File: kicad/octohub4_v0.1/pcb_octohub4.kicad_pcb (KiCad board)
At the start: 2 copper layers, 100 x 80 mm, 83 parts, among them J101 USB231ARY, J102 USB231ARY, J103 USB231ARY, J104 USB231ARY, J201 Screw_Terminal_01x02, J203 Barrel_Jack_Switch, J301 USB_C_Receptacle_USB2.0, U201 TPS259474LRPWR, U301 AMS1117-3.3, U302 USB2514B_Bi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

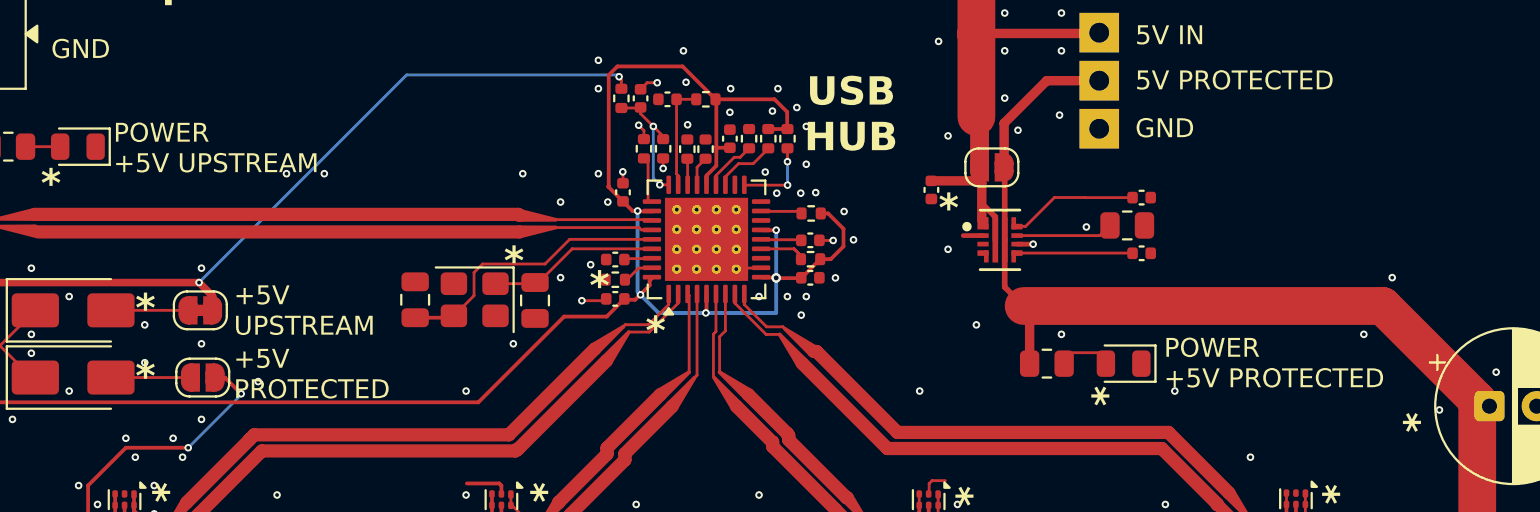
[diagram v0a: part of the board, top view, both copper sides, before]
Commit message: Add run_kicad_purge 8
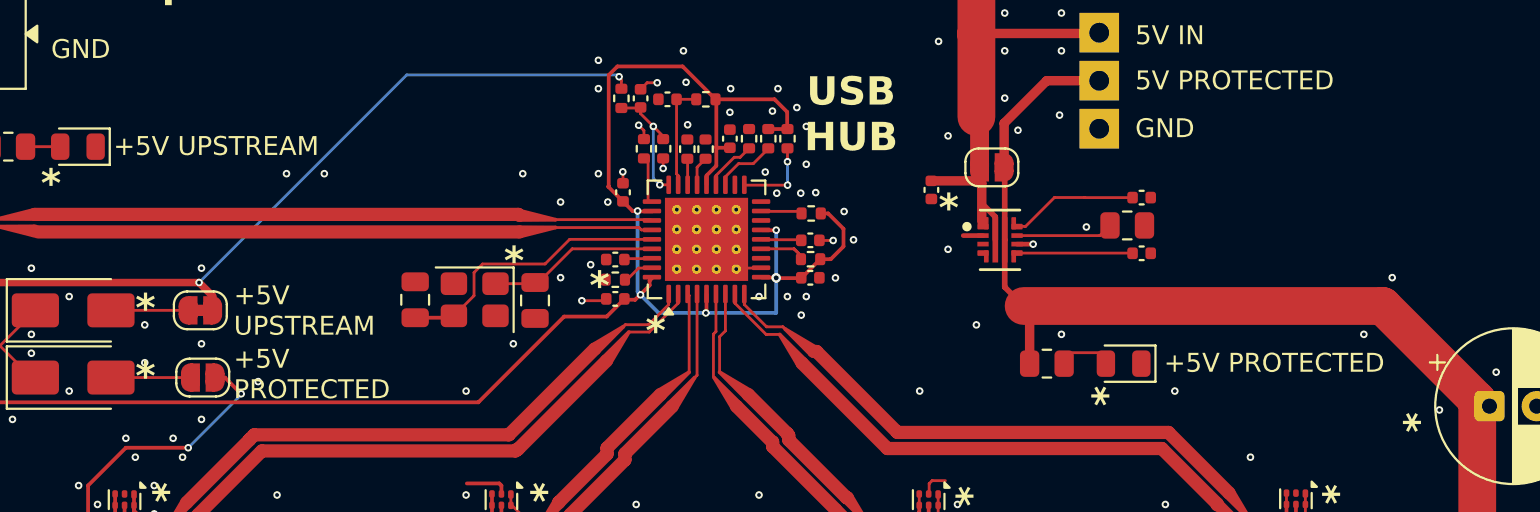
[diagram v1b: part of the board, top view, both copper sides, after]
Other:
- board text removed: "POWER +5V PROTECTED"
- board text removed: "POWER +5V UPSTREAM"
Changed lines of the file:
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@@
 			)
 		)
-		(property "Description" "19.414.67.1mm USB Connectors ROHS 4 pin USB 2.0 DC 30V 1.5 A"
+		(property "Description" "USB Connectors ROHS 4 pin USB 2.0 DC 30V 1.5 A"
 			(at 0 0 0)
 			(unlocked yes)
@@
 			)
 		)
-		(property "Datasheet_alt" "https://datasheet.lcsc.com/lcsc/2008111235_XUNPU-USB-226-BRW_C720524.pdf"
+		(property "Datasheet_alt" "https://jlcpcb.com/api/file/downloadByFileSystemAccessId/8608741080523153408"
 			(at 0 0 0)
 			(unlocked yes)
@@
 			)
 		)
-		(property "Description" "19.414.67.1mm USB Connectors ROHS 4 pin USB 2.0 DC 30V 1.5 A"
+		(property "Description" "USB Connectors ROHS 4 pin USB 2.0 DC 30V 1.5 A"
 			(at 0 0 0)
 			(unlocked yes)
@@
 			)
 		)
-		(property "Datasheet_alt" "https://datasheet.lcsc.com/lcsc/2008111235_XUNPU-USB-226-BRW_C720524.pdf"
+		(property "Datasheet_alt" "https://jlcpcb.com/api/file/downloadByFileSystemAccessId/8608741080523153408"
 			(at 0 0 0)
 			(unlocked yes)
@@
 			)
 		)
-		(property "Description" "19.414.67.1mm USB Connectors ROHS 4 pin USB 2.0 DC 30V 1.5 A"
+		(property "Description" "USB Connectors ROHS 4 pin USB 2.0 DC 30V 1.5 A"
 			(at 0 0 0)
 			(unlocked yes)
@@
 			)
 		)
-		(property "Datasheet_alt" "https://datasheet.lcsc.com/lcsc/2008111235_XUNPU-USB-226-BRW_C720524.pdf"
+		(property "Datasheet_alt" "https://jlcpcb.com/api/file/downloadByFileSystemAccessId/8608741080523153408"
 			(at 0 0 0)
 			(unlocked yes)
@@
 			)
 		)
-		(property "Description" "19.414.67.1mm USB Connectors ROHS 4 pin USB 2.0 DC 30V 1.5 A"
+		(property "Description" "USB Connectors ROHS 4 pin USB 2.0 DC 30V 1.5 A"
 			(at 0 0 0)
 			(unlocked yes)
@@
 			)
 		)
-		(property "Datasheet_alt" "https://datasheet.lcsc.com/lcsc/2008111235_XUNPU-USB-226-BRW_C720524.pdf"
+		(property "Datasheet_alt" "https://jlcpcb.com/api/file/downloadByFileSystemAccessId/8608741080523153408"
 			(at 0 0 0)
 			(unlocked yes)
@@
 		)
 	)
-	(gr_text "POWER\n+5V PROTECTED"
-		(at 133.18 74.68 0)
+	(gr_text "+5V PROTECTED"
+		(at 133.18 73.86 0)
 		(layer "F.SilkS")
 		(effects
@@
 		)
 	)
-	(gr_text "POWER\n+5V UPSTREAM"
-		(at 77.6 63.3 0)
+	(gr_text "+5V UPSTREAM"
+		(at 77.6 62.39 0)
 		(layer "F.SilkS")
 		(effects

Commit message: Add run_kicad_purge 9
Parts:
- added D208: green, LED_SMD:LED_0805_2012Metric, F.Cu at (127.0, 73.8)
- added R203: 4K7, Resistor_SMD:R_0805_2012Metric, F.Cu at (131.1, 73.8)
- moved R202 4.42 mm to (131.1, 71.6), turned to 0 degrees
- moved D207 4.35 mm to (127.0, 71.6), turned to 0 degrees
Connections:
- U201 pad 4: unconnected-(U201-PGTH-Pad4) -> Net-(D208-K)
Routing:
- net Net-(D208-K): track 0.00 -> 8.39 mm
- net Net-(D208-A): track 0.00 -> 2.21 mm
- net +5VPROTECTED: track 203.9 -> 205.3 mm
- net GND: vias 216 -> 226
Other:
- board text added: "FAULT"

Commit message: Version v0.1
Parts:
- R201: value 120 -> 680
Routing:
- net +5VIN: track 256.6 -> 255.9 mm
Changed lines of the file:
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@@
 			)
 		)
-		(property "KiCadOriginal" "MountingHole_3.2mm_M3_DIN965_Pad"
-			(at 0 0 0)
-			(layer "F.SilkS")
-			(hide yes)
-			(effects
-				(font
-					(size 1 1)
-					(thickness 0.1)
-				)
-			)
-		)
 		(property ki_fp_filters "MountingHole*Pad*")
 		(sheetname "/Power Protection/")
@@
 			)
 		)
-		(property "KiCadOriginal" "MountingHole_3.2mm_M3_DIN965_Pad"
-			(at 0 0 0)
-			(layer "F.SilkS")
-			(hide yes)
-			(effects
-				(font
-					(size 1 1)
-					(thickness 0.1)
-				)
-			)
-		)
 		(property ki_fp_filters "MountingHole*Pad*")
 		(sheetname "/Power Protection/")
@@
 			)
 		)
-		(property "KiCadOriginal" "TerminalBlock_WAGO_236-402_1x02_P5.00mm_45Degree"
-			(at 0 0 90)
-			(layer "F.SilkS")
-			(hide yes)
-			(effects
-				(font
-					(size 1 1)
-					(thickness 0.1)
-				)
-			)
-		)
 		(property ki_fp_filters "TerminalBlock*:*")
 		(sheetname "/Power Protection/")
@@
 			)
 		)
-		(property "KiCadOrigin" "BarrelJack_CUI_PJ-079BH_Horizontal"
-			(at 0 0 90)
-			(layer "F.SilkS")
-			(hide yes)
-			(effects
-				(font
-					(size 1 1)
-					(thickness 0.1)
-				)
-			)
-		)
 		(property "JLCPCB" "C319095"
 			(at 0 0 270)
@@
 			)
 		)
-		(property "Value" "120"
+		(property "Value" "680"
 			(at 0 1.65 0)
 			(layer "F.Fab")
@@
 			)
 		)
-		(property "KiCadOriginal" "MountingHole_3.2mm_M3_DIN965_Pad"
-			(at 0 0 0)
-			(layer "F.SilkS")
-			(hide yes)
-			(effects
-				(font
-					(size 1 1)
-					(thickness 0.1)
-				)
-			)
-		)
 		(property ki_fp_filters "MountingHole*Pad*")
 		(sheetname "/Power Protection/")
@@
 			)
 		)
-		(property "KiCadOriginal" "MountingHole_3.2mm_M3_DIN965_Pad"
-			(at 0 0 0)
-			(layer "F.SilkS")
-			(hide yes)
-			(effects
-				(font
-					(size 1 1)
-					(thickness 0.1)
-				)
-			)
-		)
 		(property ki_fp_filters "MountingHole*Pad*")
 		(sheetname "/Power Protection/")
@@
 	)
 	(segment
-		(start 124.26 65.99)
-		(end 124.26 66.4)
-		(width 0.3)
-		(layer "F.Cu")
-		(net 1)
-	)
-	(segment
 		(start 123.4432 63.6612)
 		(end 123.5448 63.7628)
@@
 	)
 	(segment
-		(start 124.26 66.4)
-		(end 124.26 66.76)
-		(width 0.3)
-		(layer "F.Cu")
-		(net 1)
-	)
-	(segment
 		(start 72.41 23.26)
 		(end 73.76 23.26)
@@
 		(layer "F.Cu")
 		(net 2)
-	)
-	(segment
-		(start 131.9825 73.7875)
-		(end 131.9925 73.7775)
-		(width 0.5)
-		(layer "F.Cu")
-		(net 2)

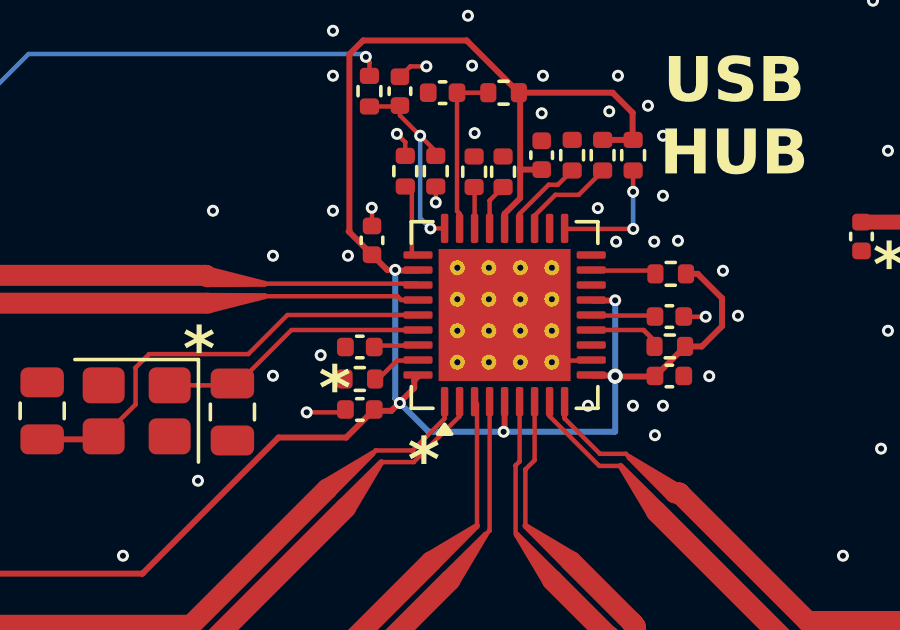
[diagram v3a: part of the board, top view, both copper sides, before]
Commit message: New via constraints: Copy usb hub footprint from tentacle v0.7
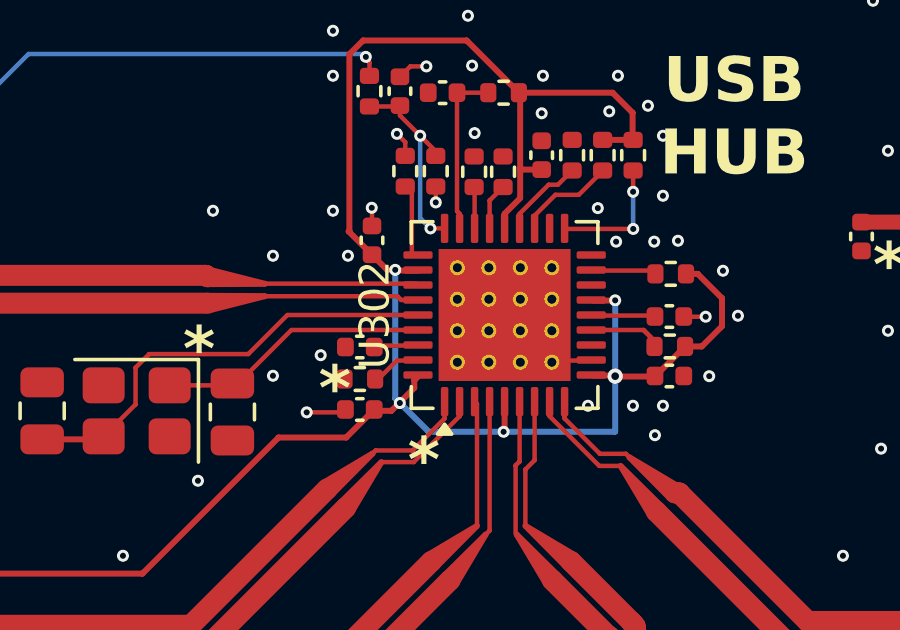
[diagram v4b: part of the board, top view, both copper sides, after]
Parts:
- U302: footprint Package_DFN_QFN:Texas_RHH0036C_VQFN-36-1EP_6x6mm_P0.5mm_EP4.4x4.4mm_ThermalVias -> 00_project_library:Texas_RHH0036C_VQFN-36-1EP_6x6mm_P0.5mm_EP4.4x4.4mm_ThermalVias
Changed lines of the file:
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@@
 		(embedded_fonts no)
 	)
-	(footprint "Package_DFN_QFN:Texas_RHH0036C_VQFN-36-1EP_6x6mm_P0.5mm_EP4.4x4.4mm_ThermalVias"
+	(footprint "00_project_library:Texas_RHH0036C_VQFN-36-1EP_6x6mm_P0.5mm_EP4.4x4.4mm_ThermalVias"
 		(layer "F.Cu")
 		(at 108.9814 66.735 90)
@@
 			(at 0 -4.33 90)
 			(layer "F.SilkS")
-			(hide yes)
 			(effects
 				(font
@@
 			(at -1.575 -1.575 90)
 			(size 0.5 0.5)
-			(drill 0.2)
+			(drill 0.3)
 			(property pad_prop_heatsink)
 			(layers "*.Cu")
@@
 			(at -1.575 -0.525 90)
 			(size 0.5 0.5)
-			(drill 0.2)
+			(drill 0.3)
 			(property pad_prop_heatsink)
 			(layers "*.Cu")
@@
 			(at -1.575 0.525 90)
 			(size 0.5 0.5)
-			(drill 0.2)
+			(drill 0.3)
 			(property pad_prop_heatsink)
 			(layers "*.Cu")
@@
 			(at -1.575 1.575 90)
 			(size 0.5 0.5)
-			(drill 0.2)
+			(drill 0.3)
 			(property pad_prop_heatsink)
 			(layers "*.Cu")
@@
 			(at -0.525 -1.575 90)
 			(size 0.5 0.5)
-			(drill 0.2)
+			(drill 0.3)
 			(property pad_prop_heatsink)
 			(layers "*.Cu")
@@
 			(at -0.525 -0.525 90)
 			(size 0.5 0.5)
-			(drill 0.2)
+			(drill 0.3)
 			(property pad_prop_heatsink)
 			(layers "*.Cu")
@@
 			(at -0.525 0.525 90)
 			(size 0.5 0.5)
-			(drill 0.2)
+			(drill 0.3)
 			(property pad_prop_heatsink)
 			(layers "*.Cu")
@@
 			(at -0.525 1.575 90)
 			(size 0.5 0.5)
-			(drill 0.2)
+			(drill 0.3)
 			(property pad_prop_heatsink)
 			(layers "*.Cu")
@@
 			(at 0.525 -1.575 90)
 			(size 0.5 0.5)
-			(drill 0.2)
+			(drill 0.3)
 			(property pad_prop_heatsink)
 			(layers "*.Cu")
@@
 			(at 0.525 -0.525 90)
 			(size 0.5 0.5)
-			(drill 0.2)
+			(drill 0.3)
 			(property pad_prop_heatsink)
 			(layers "*.Cu")
@@
 			(at 0.525 0.525 90)
 			(size 0.5 0.5)
-			(drill 0.2)
+			(drill 0.3)
 			(property pad_prop_heatsink)
 			(layers "*.Cu")
@@
 			(at 0.525 1.575 90)
 			(size 0.5 0.5)
-			(drill 0.2)
+			(drill 0.3)
 			(property pad_prop_heatsink)
 			(layers "*.Cu")
@@
 			(at 1.575 -1.575 90)
 			(size 0.5 0.5)
-			(drill 0.2)
+			(drill 0.3)
 			(property pad_prop_heatsink)
 			(layers "*.Cu")
@@
 			(at 1.575 -0.525 90)
 			(size 0.5 0.5)
-			(drill 0.2)
+			(drill 0.3)
 			(property pad_prop_heatsink)
 			(layers "*.Cu")
@@
 			(at 1.575 0.525 90)
 			(size 0.5 0.5)
-			(drill 0.2)
+			(drill 0.3)
 			(property pad_prop_heatsink)
 			(layers "*.Cu")
@@
 			(at 1.575 1.575 90)
 			(size 0.5 0.5)
-			(drill 0.2)
-			(property pad_prop_heatsink)
-			(layers "*.Cu")
+			(drill 0.3)
+			(property pad_prop_heatsink)
+			(layers "*.Cu")

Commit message: Version v0.1. Manually fix all violations.
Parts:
- moved R302 0.39 mm to (68.7, 64.4)
